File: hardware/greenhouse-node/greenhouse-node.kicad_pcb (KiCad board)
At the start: 2 copper layers, 90.2 x 69.8 mm, 54 parts, among them J1 Conn_01x12_Male, J2 Conn_01x02_Male, J3 Conn_01x02_Male, J4 Conn_01x02_Male, J5 Conn_01x04_Male, J6 Conn_01x05_Female, J7 Conn_01x02_Male, Q1 BC549C, Q2 BC549C, Q3 IRF9530N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

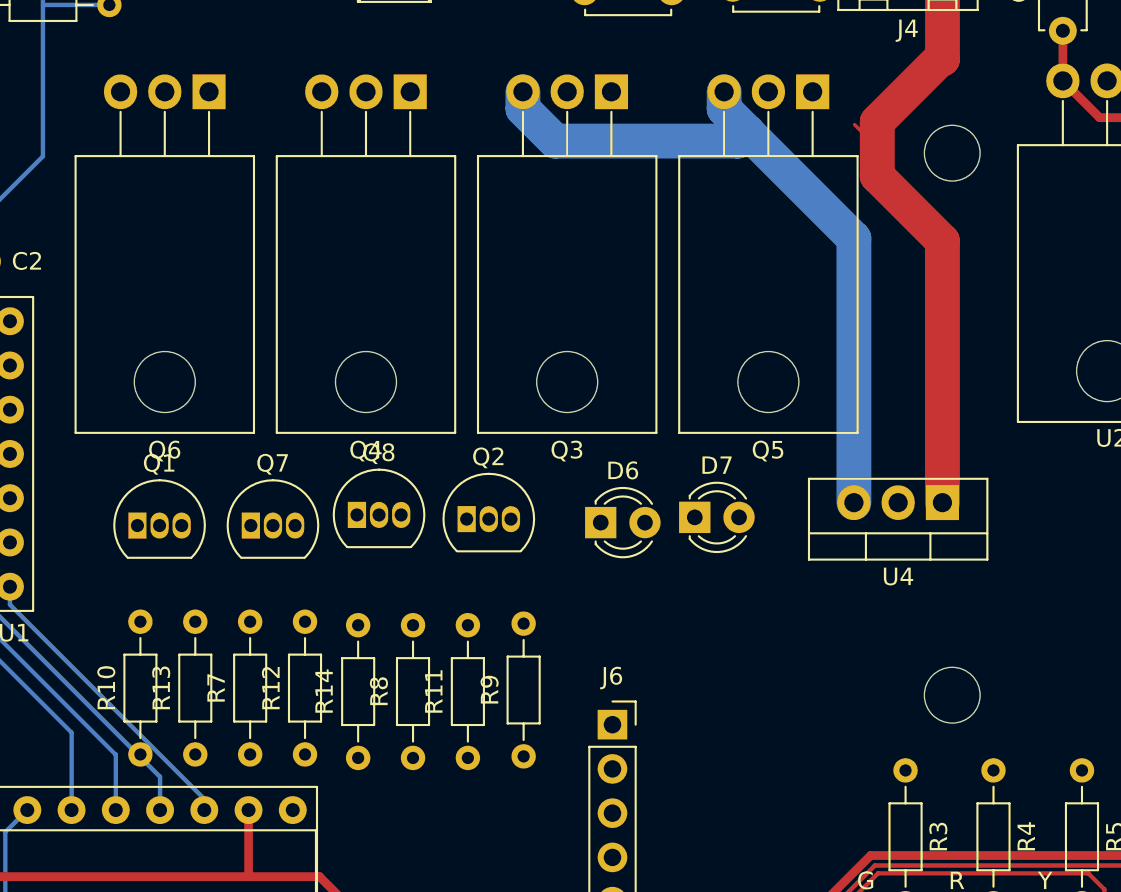
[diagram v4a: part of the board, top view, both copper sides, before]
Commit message: Joined some tracks
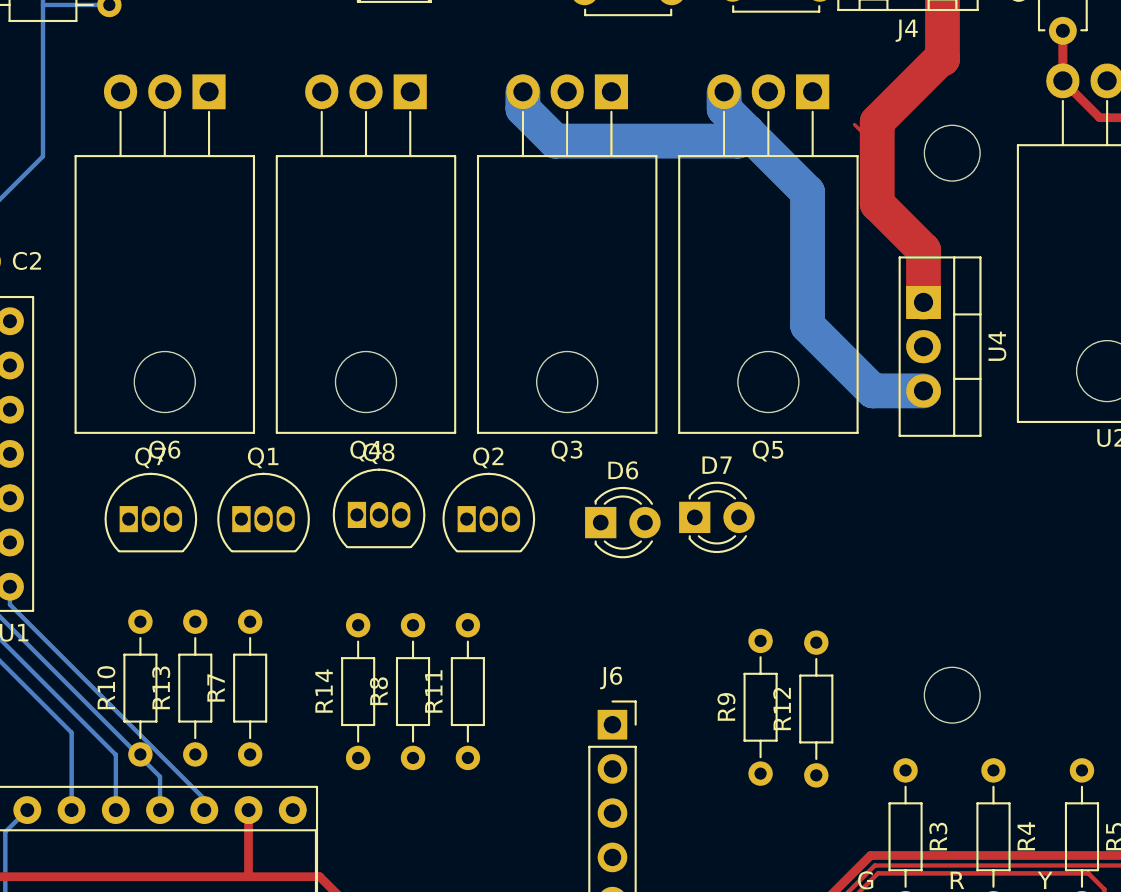
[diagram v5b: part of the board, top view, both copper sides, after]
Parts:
- moved R12 29.4 mm to (125.8, 81.3)
- moved R9 13.6 mm to (122.6, 81.2)
- moved U4 11.5 mm to (132.0, 54.2), turned to -90 degrees
- moved Q7 7.02 mm to (86.3, 66.6)
- moved Q1 5.98 mm to (92.8, 66.6)
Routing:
- net +12V: track 43.9 -> 32.0 mm
- net +10V: track 41.5 -> 38.4 mm
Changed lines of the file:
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@@
   )
   (footprint "Resistor_THT:R_Axial_DIN0204_L3.6mm_D1.6mm_P7.62mm_Horizontal" (layer "F.Cu")
-    (at 96.45 80.11 90)
+    (at 125.8 81.31 90)
     (descr "Resistor, Axial_DIN0204 series, Axial, Horizontal, pin pitch=7.62mm, 0.167W, length*diameter=3.6*1.6mm^2, http://cdn-reichelt.de/documents/datenblatt/B400/1_4W%23YAG.pdf")
     (tags "Resistor Axial_DIN0204 series Axial Horizontal pin pitch 7.62mm 0.167W length 3.6mm diameter 1.6mm")
@@
   )
   (footprint "Resistor_THT:R_Axial_DIN0204_L3.6mm_D1.6mm_P7.62mm_Horizontal" (layer "F.Cu")
-    (at 109 80.22 90)
+    (at 122.6 81.21 90)
     (descr "Resistor, Axial_DIN0204 series, Axial, Horizontal, pin pitch=7.62mm, 0.167W, length*diameter=3.6*1.6mm^2, http://cdn-reichelt.de/documents/datenblatt/B400/1_4W%23YAG.pdf")
     (tags "Resistor Axial_DIN0204 series Axial Horizontal pin pitch 7.62mm 0.167W length 3.6mm diameter 1.6mm")
@@
   )
   (footprint "Package_TO_SOT_THT:TO-92_Inline" (layer "F.Cu")
-    (at 86.83 66.97)
+    (at 92.8 66.6)
     (descr "TO-92 leads in-line, narrow, oval pads, drill 0.75mm (see NXP sot054_po.pdf)")
     (tags "to-92 sc-43 sc-43a sot54 PA33 transistor")
@@
   )
   (footprint "Package_TO_SOT_THT:TO-220-3_Vertical" (layer "F.Cu")
-    (at 133.04 65.655 180)
+    (at 131.955 54.16 -90)
     (descr "TO-220-3, Vertical, RM 2.54mm, see https://www.vishay.com/docs/66542/to-220-1.pdf")
     (tags "TO-220-3 Vertical RM 2.54mm")
@@
     (property "Sheetname" "")
     (attr through_hole)
-    (fp_text reference "U4" (at 2.54 -4.27) (layer "F.SilkS")
-      (effects (font (size 1 1) (thickness 0.15)))
-    )
-    (fp_text value "L7810" (at 2.54 2.5) (layer "F.Fab")
-      (effects (font (size 1 1) (thickness 0.15)))
-    )
-    (fp_text user "${REFERENCE}" (at 2.54 -4.27) (layer "F.Fab")
+    (fp_text reference "U4" (at 2.54 -4.27 -270) (layer "F.SilkS")
+      (effects (font (size 1 1) (thickness 0.15)))
+    )
+    (fp_text value "L7810" (at 2.54 2.5 -270) (layer "F.Fab")
+      (effects (font (size 1 1) (thickness 0.15)))
+    )
+    (fp_text user "${REFERENCE}" (at 2.54 -4.27 -270) (layer "F.Fab")
       (effects (font (size 1 1) (thickness 0.15)))
     )
@@
     (fp_line (start -2.46 -1.88) (end 7.54 -1.88) (layer "F.Fab") (width 0.1))
     (fp_line (start 7.54 1.25) (end 7.54 -3.15) (layer "F.Fab") (width 0.1))
-    (pad "1" thru_hole rect (at 0 0 180) (size 1.905 2) (drill 1.1) (layers *.Cu *.Mask)
+    (pad "1" thru_hole rect (at 0 0 270) (size 1.905 2) (drill 1.1) (layers *.Cu *.Mask)
       (net 6 "+12V") (pinfunction "IN") (pintype "power_in"))
-    (pad "2" thru_hole oval (at 2.54 0 180) (size 1.905 2) (drill 1.1) (layers *.Cu *.Mask)
+    (pad "2" thru_hole oval (at 2.54 0 270) (size 1.905 2) (drill 1.1) (layers *.Cu *.Mask)
       (net 2 "GND") (pinfunction "GND") (pintype "power_in"))
-    (pad "3" thru_hole oval (at 5.08 0 180) (size 1.905 2) (drill 1.1) (layers *.Cu *.Mask)
+    (pad "3" thru_hole oval (at 5.08 0 270) (size 1.905 2) (drill 1.1) (layers *.Cu *.Mask)
       (net 7 "+10V") (pinfunction "OUT") (pintype "power_out"))
     (model "${KICAD6_3DMODEL_DIR}/Package_TO_SOT_THT.3dshapes/TO-220-3_Vertical.wrl"
@@
   )
   (footprint "Package_TO_SOT_THT:TO-92_Inline" (layer "F.Cu")
-    (at 93.34 66.97)
+    (at 86.33 66.6)
     (descr "TO-92 leads in-line, narrow, oval pads, drill 0.75mm (see NXP sot054_po.pdf)")
     (tags "to-92 sc-43 sc-43a sot54 PA33 transistor")
@@
   (segment (start 77.978 87.122) (end 93.218 87.122) (width 0.5) (layer "F.Cu") (net 1))
   (segment (start 64.897 46.465) (end 61.324 46.465) (width 0.5) (layer "F.Cu") (net 1))
+  (segment (start 129.3 43.8) (end 129.3 48.5) (width 2) (layer "F.Cu") (net 6))
   (segment (start 137.384 29.718) (end 134.949 32.153) (width 0.5) (layer "F.Cu") (net 6))
-  (segment (start 132.916 40.184) (end 129.3 43.8) (width 2) (layer "F.Cu") (net 6))
   (segment (start 133.044 32.153) (end 133.044 40.184) (width 2) (layer "F.Cu") (net 6))
-  (segment (start 133.044 40.184) (end 132.916 40.184) (width 2) (layer "F.Cu") (net 6))
   (segment (start 128.524 44.48196) (end 128.00002 43.95798) (width 0.2) (layer "F.Cu") (net 6))
   (segment (start 138.557 29.718) (end 137.384 29.718) (width 0.5) (layer "F.Cu") (net 6))
-  (segment (start 129.3 46.9) (end 133.04 50.64) (width 2) (layer "F.Cu") (net 6))
-  (segment (start 133.04 50.64) (end 133.04 65.655) (width 2) (layer "F.Cu") (net 6))
+  (segment (start 131.955 54.16) (end 131.955 51.155) (width 2) (layer "F.Cu") (net 6))
+  (segment (start 132.916 40.184) (end 129.3 43.8) (width 2) (layer "F.Cu") (net 6))
   (segment (start 134.949 32.153) (end 133.044 32.153) (width 0.5) (layer "F.Cu") (net 6))
-  (segment (start 129.3 43.8) (end 129.3 46.9) (width 2) (layer "F.Cu") (net 6))
-  (segment (start 127.96 50.495179) (end 121.83241 44.36759) (width 2) (layer "B.Cu") (net 7))
+  (segment (start 129.3 48.5) (end 131.955 51.155) (width 2) (layer "F.Cu") (net 6))
+  (segment (start 133.044 40.184) (end 132.916 40.184) (width 2) (layer "F.Cu") (net 6))
+  (segment (start 129.05 59.24) (end 131.955 59.24) (width 2) (layer "B.Cu") (net 7))
   (segment (start 108.96 43.045179) (end 110.814821 44.9) (width 2) (layer "B.Cu") (net 7))
   (segment (start 121.3 44.9) (end 121.83241 44.36759) (width 2) (layer "B.Cu") (net 7))
+  (segment (start 125.3 47.83518) (end 125.3 55.49) (width 2) (layer "B.Cu") (net 7))
   (segment (start 110.814821 44.9) (end 121.3 44.9) (width 2) (layer "B.Cu") (net 7))
-  (segment (start 127.96 65.655) (end 127.96 50.495179) (width 2) (layer "B.Cu") (net 7))
+  (segment (start 125.3 55.49) (end 129.05 59.24) (width 2) (layer "B.Cu") (net 7))
+  (segment (start 121.83241 44.36759) (end 125.3 47.83518) (width 2) (layer "B.Cu") (net 7))
   (segment (start 108.96 42.07) (end 108.96 43.045179) (width 2) (layer "B.Cu") (net 7))
   (segment (start 120.51 43.045179) (end 120.51 42.07) (width 2) (layer "B.Cu") (net 7))

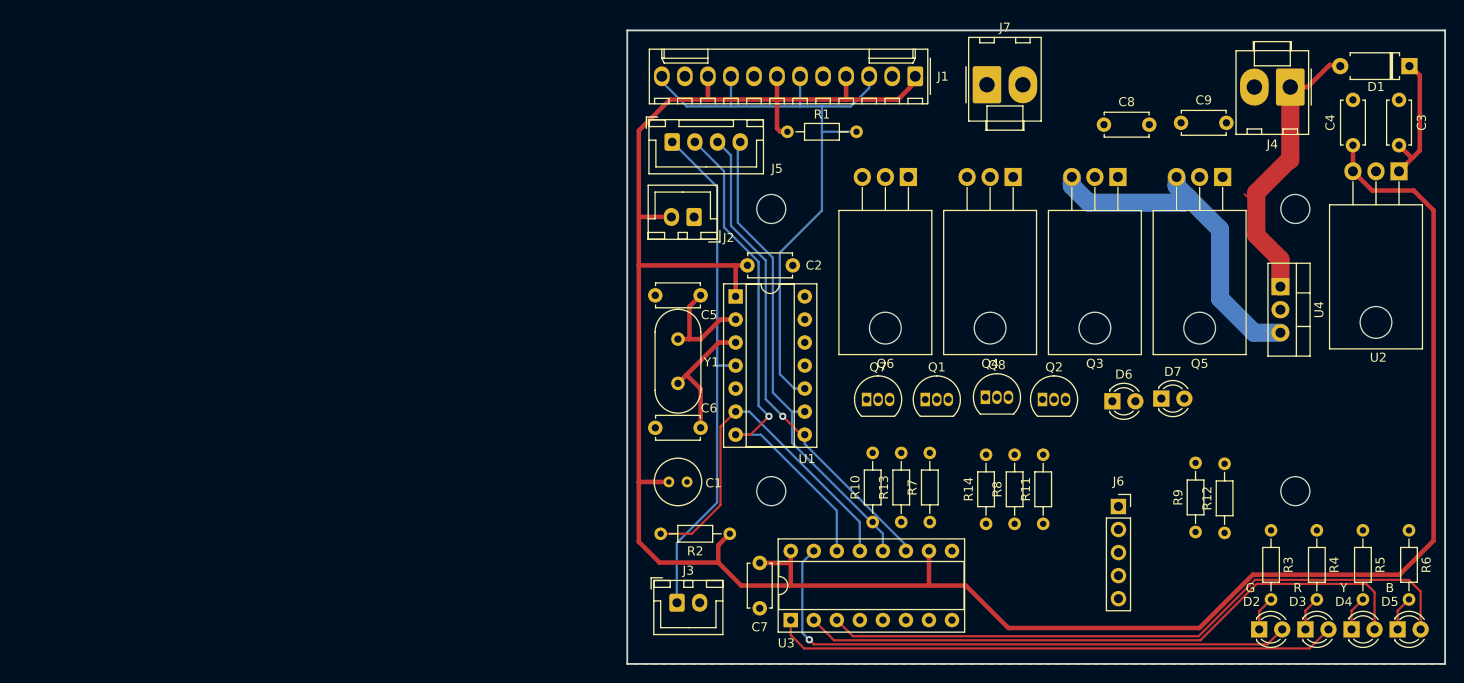
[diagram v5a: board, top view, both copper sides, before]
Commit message: Finish traces for node
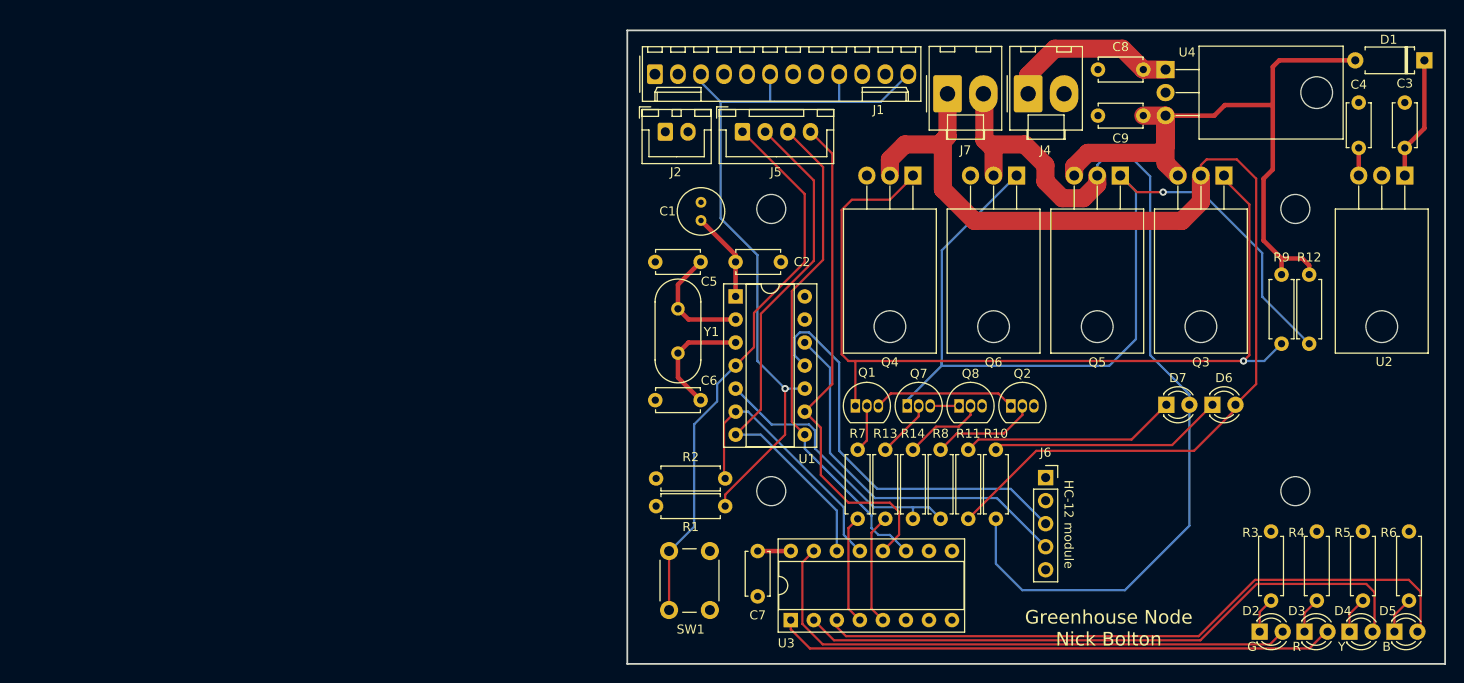
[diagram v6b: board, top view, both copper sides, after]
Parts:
- removed J3: Conn_01x02_Male, Connector_JST:JST_XH_B2B-XH-A_1x02_P2.50mm_Vertical
- added SW1: SW_Push, Button_Switch_THT:SW_PUSH_6mm, F.Cu at (64.6, 89.8)
- R1, R10, R11, R12, R13, R14, R2, R3, R4, R5, R6, R7, R8, R9: footprint Resistor_THT:R_Axial_DIN0204_L3.6mm_D1.6mm_P7.62mm_Horizontal -> Resistor_THT:R_Axial_DIN0207_L6.3mm_D2.5mm_P7.62mm_Horizontal
- U4: footprint Package_TO_SOT_THT:TO-220-3_Vertical -> Package_TO_SOT_THT:TO-220-3_Horizontal_TabDown
- moved R1 43.7 mm to (63.1, 78.4)
- moved C1 29.0 mm to (68.1, 46.9), turned to 90 degrees
- moved J4 28.9 mm to (104.1, 32.9), turned to 0 degrees
- moved J1 28.7 mm to (63.0, 30.7), turned to 0 degrees
- moved U4 27.1 mm to (119.3, 30.2)
- moved R12 22.8 mm to (135.1, 60.5)
- moved R9 22.8 mm to (132.1, 60.5)
- moved R10 13.6 mm to (100.6, 79.8)
- moved Q6 11.9 mm to (102.9, 41.9)
- moved Q3 11.7 mm to (125.7, 41.9)
- moved R8 11.6 mm to (94.5, 72.1), turned to -90 degrees
- moved R14 11.5 mm to (91.4, 72.1), turned to -90 degrees
- moved Q5 11.3 mm to (114.3, 41.9)
- moved R7 11.3 mm to (85.3, 72.1), turned to -90 degrees
- moved Q4 11.1 mm to (91.4, 41.9)
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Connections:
- U3 pad 4: Motor_B -> Motor_A
- U3 pad 5: Motor_A -> Motor_B
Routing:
- net +5V: track 272.8 -> 16.7 mm
- net /Motor_1: track 0.00 -> 122.7 mm
- net /Motor_2: track 0.00 -> 105.6 mm
- net Net-(Q5-Pad1): track 0.00 -> 103.5 mm, vias 0 -> 1
- net Net-(Q1-Pad1): track 0.00 -> 101.8 mm, vias 0 -> 1
- net /SR_CLK: track 0.00 -> 55.2 mm
- net /SR_RCLK: track 105.8 -> 56.2 mm, vias 1 -> 0
- net /RAD_RX: track 0.00 -> 45.9 mm
- net /RAD_TX: track 0.00 -> 41.4 mm
- net +10V: track 38.4 -> 75.2 mm
- net Motor_PWM: track 0.00 -> 31.0 mm
- net Net-(D6-Pad1): track 0.00 -> 25.9 mm
- net Net-(D7-Pad1): track 0.00 -> 23.9 mm
- net Net-(Q1-Pad3): track 0.00 -> 15.7 mm
- net /OneWire: track 71.4 -> 84.4 mm, vias 0 -> 1
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- added copper zone on In1.Cu, net +5V
- added copper zone on In2.Cu, net GND
- removed copper zone on B.Cu, net GND
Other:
- copper layers 2 -> 4
- board text added: "Greenhouse Node Nick Bolton"
- board text added: "HC-12 module"

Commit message: Change N/P-MOS parts
Also added some no-connects
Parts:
- Q3, Q5: value IRF9530N -> IRF4905
- Q4, Q6: value IRF530N -> FDP7030BL
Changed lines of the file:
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@@
       (net 32 "Motor_B") (pinfunction "QF") (pintype "tri_state"))
     (pad "6" thru_hole oval (at 0 12.7 90) (size 1.6 1.6) (drill 0.8) (layers *.Cu *.Mask)
-      (net 26 "unconnected-(U3-Pad6)") (pinfunction "QG") (pintype "tri_state"))
+      (net 26 "unconnected-(U3-Pad6)") (pinfunction "QG") (pintype "tri_state+no_connect"))
     (pad "7" thru_hole oval (at 0 15.24 90) (size 1.6 1.6) (drill 0.8) (layers *.Cu *.Mask)
-      (net 27 "unconnected-(U3-Pad7)") (pinfunction "QH") (pintype "tri_state"))
+      (net 27 "unconnected-(U3-Pad7)") (pinfunction "QH") (pintype "tri_state+no_connect"))
     (pad "8" thru_hole oval (at 0 17.78 90) (size 1.6 1.6) (drill 0.8) (layers *.Cu *.Mask)
       (net 2 "GND") (pinfunction "GND") (pintype "power_in"))
     (pad "9" thru_hole oval (at 7.62 17.78 90) (size 1.6 1.6) (drill 0.8) (layers *.Cu *.Mask)
-      (net 28 "unconnected-(U3-Pad9)") (pinfunction "QH'") (pintype "output"))
+      (net 28 "unconnected-(U3-Pad9)") (pinfunction "QH'") (pintype "output+no_connect"))
     (pad "10" thru_hole oval (at 7.62 15.24 90) (size 1.6 1.6) (drill 0.8) (layers *.Cu *.Mask)
       (net 1 "+5V") (pinfunction "~{SRCLR}") (pintype "input"))
@@
       (net 16 "/RAD_TX") (pinfunction "PA1") (pintype "bidirectional"))
     (pad "13" thru_hole oval (at 7.62 2.54) (size 1.6 1.6) (drill 0.8) (layers *.Cu *.Mask)
-      (net 38 "unconnected-(U1-Pad13)") (pinfunction "AREF/PA0") (pintype "bidirectional"))
+      (net 38 "unconnected-(U1-Pad13)") (pinfunction "AREF/PA0") (pintype "bidirectional+no_connect"))
     (pad "14" thru_hole oval (at 7.62 0) (size 1.6 1.6) (drill 0.8) (layers *.Cu *.Mask)
       (net 2 "GND") (pinfunction "GND") (pintype "power_in"))
@@
       (effects (font (size 1 1) (thickness 0.15)))
     )
-    (fp_text value "IRF530N" (at 2.54 -12.192) (layer "F.Fab")
+    (fp_text value "FDP7030BL" (at 2.54 -12.192) (layer "F.Fab")
       (effects (font (size 1 1) (thickness 0.15)))
     )
@@
       (effects (font (size 1 1) (thickness 0.15)))
     )
-    (fp_text value "IRF9530N" (at 2.54 -12.192) (layer "F.Fab")
+    (fp_text value "IRF4905" (at 2.54 -12.192) (layer "F.Fab")
       (effects (font (size 1 1) (thickness 0.15)))
     )
@@
       (effects (font (size 1 1) (thickness 0.15)))
     )
-    (fp_text value "IRF530N" (at 2.54 -12.192) (layer "F.Fab")
+    (fp_text value "FDP7030BL" (at 2.54 -12.192) (layer "F.Fab")
       (effects (font (size 1 1) (thickness 0.15)))
     )
@@
       (effects (font (size 1 1) (thickness 0.15)))
     )
-    (fp_text value "IRF9530N" (at 2.54 -12.192) (layer "F.Fab")
-      (effects (font (size 1 1) (thickness 0.15)))
-    )
+    (fp_text value "IRF4905" (at 2.54 -12.192) (layer "F.Fab")
+      (effects (font (size 1 1) (thickness 0.15)))
+    )
